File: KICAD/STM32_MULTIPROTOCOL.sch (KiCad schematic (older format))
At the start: 76 parts, among them T1 TestPoint, T10 TestPoint, T11 TestPoint, T12 TestPoint, T13 TestPoint, T14 TestPoint, T2 TestPoint, T3 TestPoint, T4 TestPoint, T5 TestPoint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

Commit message: uart,spi,iic pins init in input mode. USB enable fixed.
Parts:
- added R24: 1.5k, Resistor_SMD:R_0805_2012Metric_Pad1.15x1.40mm_HandSolder, symbol Device:R
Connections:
- net USB_DATA+: now also R24.2
- net at U2.43 (PA10): now also R24.1
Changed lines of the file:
@@
 	1    0    0    -1
 $EndComp
-Text GLabel 9200 2350 2    50   Input ~ 0
+Text GLabel 10300 2350 2    50   Input ~ 0
 USB_DATA+
-Text GLabel 9200 2250 2    50   Input ~ 0
+Text GLabel 10300 2250 2    50   Input ~ 0
 USB_DATA-
 $Comp
@@
 Connection ~ 8400 850
 Wire Wire Line
-	9200 2250 9000 2250
-Wire Wire Line
-	9000 2350 9200 2350
+	10300 2250 9000 2250
+Wire Wire Line
+	9000 2350 9950 2350
 Text GLabel 9250 1350 2    50   Input ~ 0
 UART2_TX_PA2_PIN16
@@
 	4950 7150 6850 7150
 $Comp
-L Device:R R21
-U 1 1 60ADF8C6
-P 5750 7250
-F 0 "R21" V 5750 7250 50  0000 C CNN
-F 1 "100R" V 5866 7250 50  0001 C CNN
-F 2 "Resistor_SMD:R_0805_2012Metric_Pad1.15x1.40mm_HandSolder" V 5680 7250 50  0001 C CNN
-F 3 "~" H 5750 7250 50  0001 C CNN
-	1    5750 7250
-	0    -1   -1   0
-$EndComp
-Wire Wire Line
-	5150 7250 5600 7250
-Connection ~ 5150 7250
-Wire Wire Line
-	5900 7250 6300 7250
-$Comp
 L Connector:TestPoint T13
 U 1 1 60B0CABD
@@
 P 5200 5500
 F 0 "R22" V 5200 5500 50  0000 C CNN
-F 1 "10kR" V 5316 5500 50  0001 C CNN
+F 1 "10kR" V 5316 5500 50  0000 C CNN
 F 2 "Resistor_SMD:R_0805_2012Metric_Pad1.15x1.40mm_HandSolder" V 5130 5500 50  0001 C CNN
 F 3 "~" H 5200 5500 50  0001 C CNN
@@
 P 5000 5500
 F 0 "R23" V 5000 5500 50  0000 C CNN
-F 1 "10kR" V 5116 5500 50  0001 C CNN
+F 1 "10kR" V 4900 5500 50  0000 C CNN
 F 2 "Resistor_SMD:R_0805_2012Metric_Pad1.15x1.40mm_HandSolder" V 4930 5500 50  0001 C CNN
 F 3 "~" H 5000 5500 50  0001 C CNN
@@
 U 1 1 6050A09D
 P 10250 6200
-F 0 "CF4" H 10365 6246 50  0000 L CNN
-F 1 "22pF" H 10365 6155 50  0000 L CNN
+F 0 "CF4" V 10450 6150 50  0000 L CNN
+F 1 "22pF" V 10365 6155 50  0000 L CNN
 F 2 "Resistor_SMD:R_0402_1005Metric" H 10288 6050 50  0001 C CNN
 F 3 "~" H 10250 6200 50  0001 C CNN
@@
 U 1 1 6050AC37
 P 10300 5750
-F 0 "CF3" H 10415 5796 50  0000 L CNN
-F 1 "22pF" H 10415 5705 50  0000 L CNN
+F 0 "CF3" V 10500 5700 50  0000 L CNN
+F 1 "22pF" V 10415 5705 50  0000 L CNN
 F 2 "Resistor_SMD:R_0402_1005Metric" H 10338 5600 50  0001 C CNN
 F 3 "~" H 10300 5750 50  0001 C CNN
@@
 	8600 850  8500 850
 Connection ~ 8500 850
+Connection ~ 5150 7250
+Wire Wire Line
+	5900 7250 6300 7250
+Wire Wire Line
+	5150 7250 5600 7250
+$Comp
+L Device:R R21
+U 1 1 60ADF8C6
+P 5750 7250
+F 0 "R21" V 5750 7250 50  0000 C CNN
+F 1 "100R" V 5866 7250 50  0001 C CNN
+F 2 "Resistor_SMD:R_0805_2012Metric_Pad1.15x1.40mm_HandSolder" V 5680 7250 50  0001 C CNN
+F 3 "~" H 5750 7250 50  0001 C CNN
+	1    5750 7250
+	0    -1   -1   0
+$EndComp
+Wire Wire Line
+	9550 2150 9950 2150
+$Comp
+L Device:R R24
+U 1 1 61A28BFD
+P 9400 2150
+F 0 "R24" V 9400 2150 50  0000 C CNN
+F 1 "1.5k" V 9516 2150 50  0000 C CNN
+F 2 "Resistor_SMD:R_0805_2012Metric_Pad1.15x1.40mm_HandSolder" V 9330 2150 50  0001 C CNN
+F 3 "~" H 9400 2150 50  0001 C CNN
+	1    9400 2150
+	0    -1   -1   0
+$EndComp
+Wire Wire Line
+	9000 2150 9250 2150
+Wire Wire Line
+	9950 2150 9950 2350
+Connection ~ 9950 2350
+Wire Wire Line
+	9950 2350 10300 2350
 $EndSCHEMATC

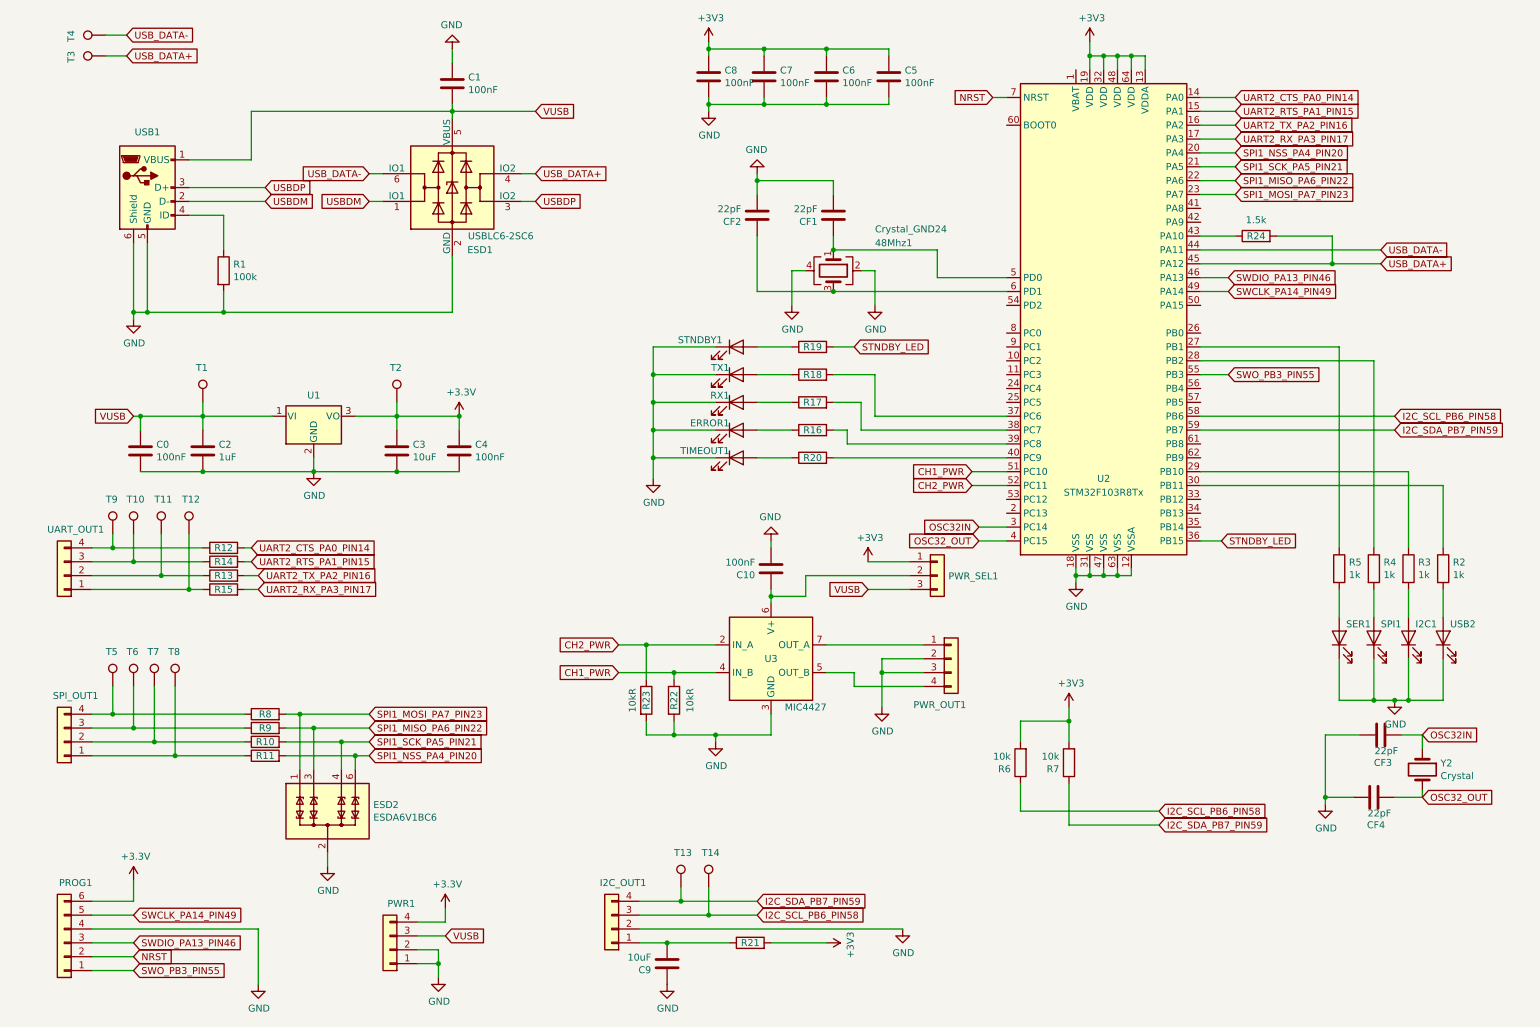
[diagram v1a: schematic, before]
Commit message: added command "stm-testled" for soldering, added schematic.pdf
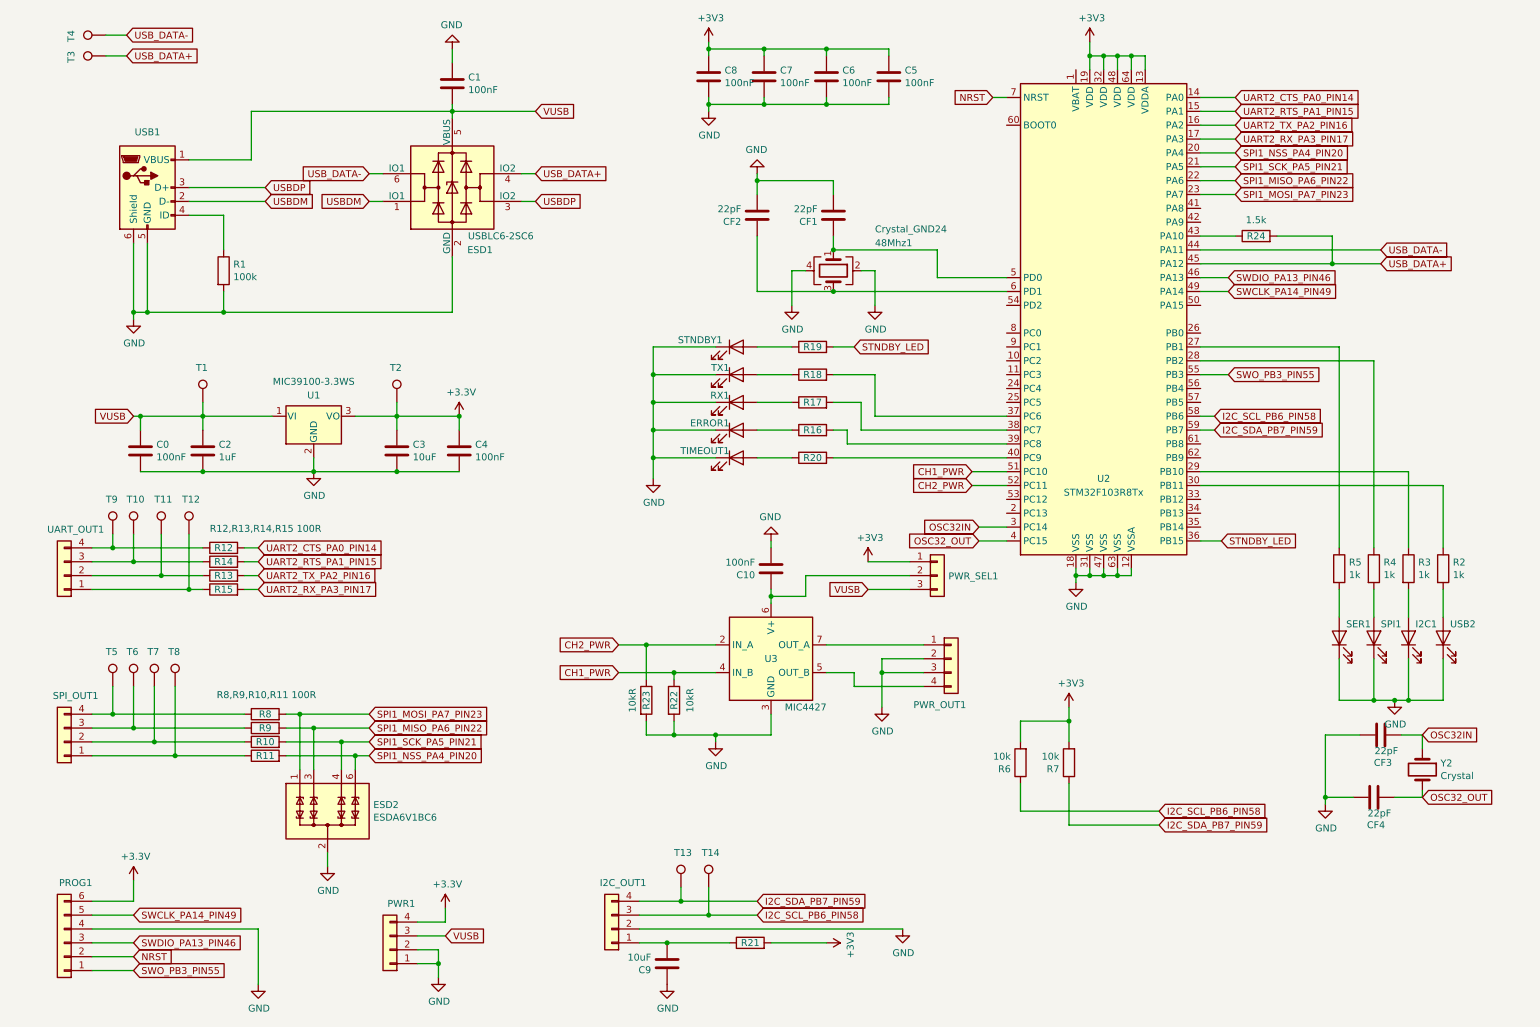
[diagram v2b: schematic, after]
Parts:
- U1: value MCP1703A-1202_SOT223 -> MIC39100-3.3WS
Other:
- note added: "R12,R13,R14,R15 100R"
- note added: "R8,R9,R10,R11 100R"
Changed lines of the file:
@@
 Wire Wire Line
 	9250 1450 9000 1450
-Text GLabel 10400 3550 2    50   Input ~ 0
+Text GLabel 9100 3550 2    50   Input ~ 0
 I2C_SDA_PB7_PIN59
-Text GLabel 10400 3450 2    50   Input ~ 0
+Text GLabel 9100 3450 2    50   Input ~ 0
 I2C_SCL_PB6_PIN58
 $Comp
@@
 P 2600 3450
 F 0 "U1" H 2600 3601 50  0000 C CNN
-F 1 "MCP1703A-1202_SOT223" H 2600 3601 50  0001 C CNN
+F 1 "MIC39100-3.3WS" H 2600 3700 50  0000 C CNN
 F 2 "Package_TO_SOT_SMD:SOT-223-3_TabPin2" H 2600 3650 50  0001 C CNN
 F 3 "http://ww1.microchip.com/downloads/en/DeviceDoc/20005122B.pdf" H 2600 3400 50  0001 C CNN
@@
 Text GLabel 2200 4700 2    50   Input ~ 0
 UART2_RX_PA3_PIN17
-Text GLabel 2150 4400 2    50   Input ~ 0
+Text GLabel 2200 4400 2    50   Input ~ 0
 UART2_CTS_PA0_PIN14
-Text GLabel 2150 4500 2    50   Input ~ 0
+Text GLabel 2200 4500 2    50   Input ~ 0
 UART2_RTS_PA1_PIN15
 Wire Wire Line
@@
 $EndComp
 Wire Wire Line
-	10400 3450 9000 3450
-Wire Wire Line
-	9000 3550 10400 3550
+	9100 3450 9000 3450
+Wire Wire Line
+	9000 3550 9100 3550
 Text GLabel 8700 6400 2    50   Input ~ 0
 I2C_SDA_PB7_PIN59
@@
 	2100 4700 2200 4700
 Wire Wire Line
-	2100 4400 2150 4400
-Wire Wire Line
-	2100 4500 2150 4500
+	2100 4400 2200 4400
+Wire Wire Line
+	2100 4500 2200 4500
 Wire Wire Line
 	3200 3350 3200 3450
@@
 Wire Wire Line
 	9950 2350 10300 2350
+Text Notes 1850 4300 0    50   ~ 0
+R12,R13,R14,R15 100R
+Text Notes 1900 5500 0    50   ~ 0
+R8,R9,R10,R11 100R
 $EndSCHEMATC

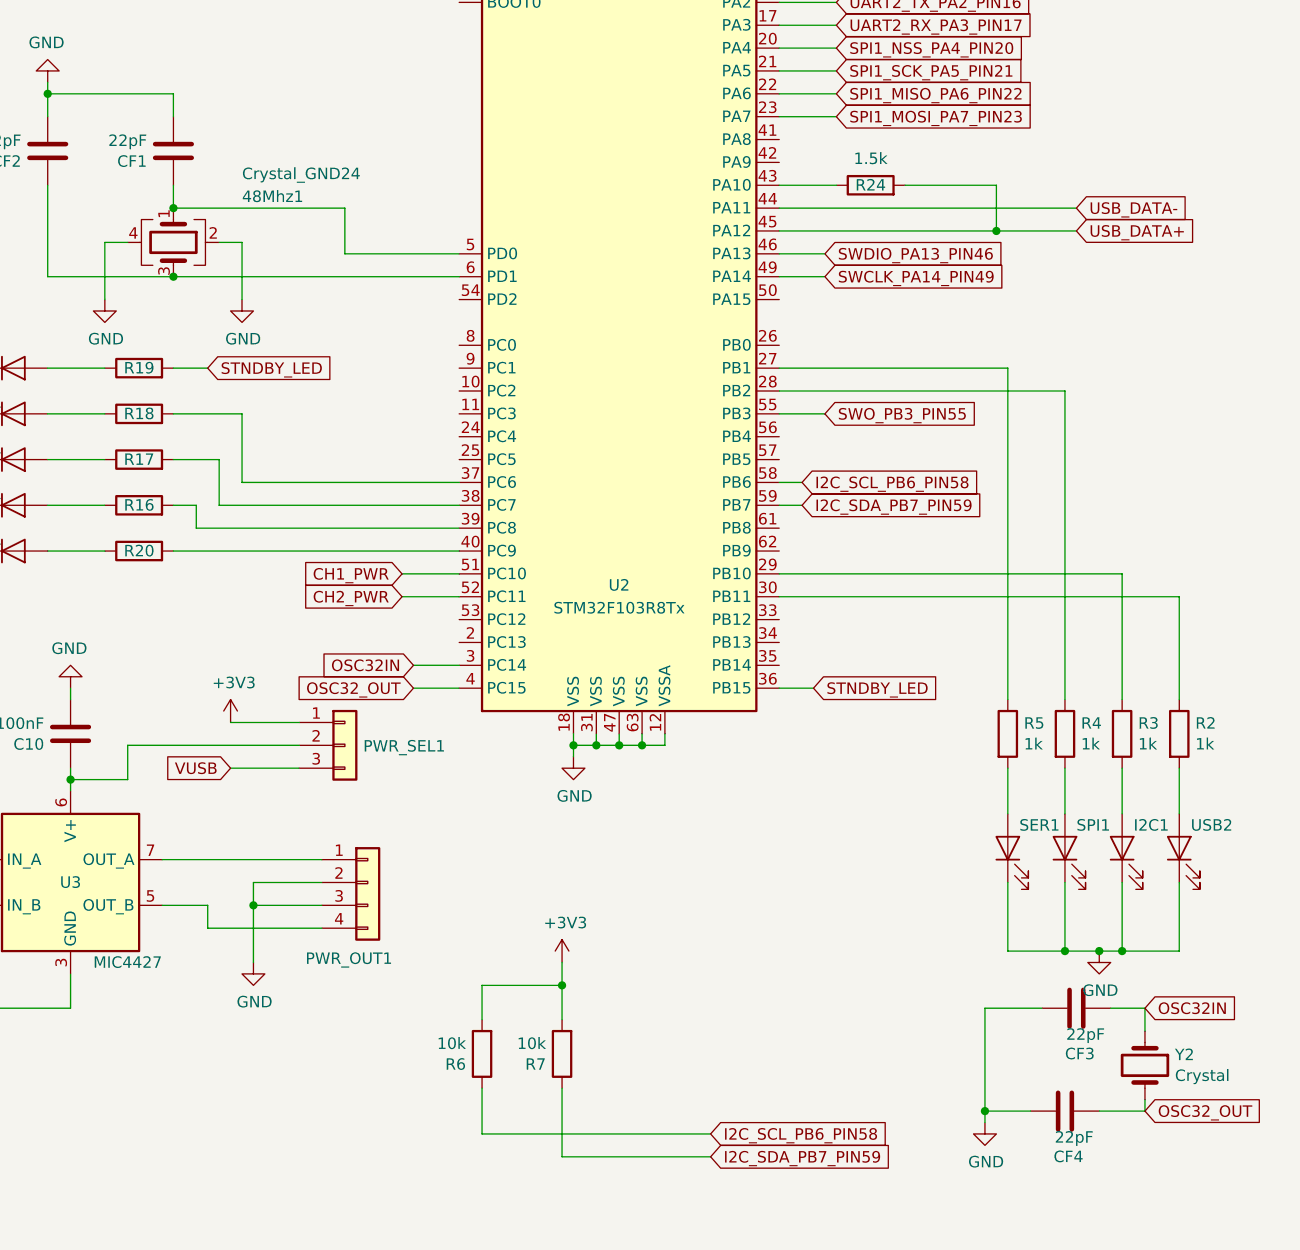
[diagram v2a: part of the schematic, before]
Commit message: added detailed BOM of the boards
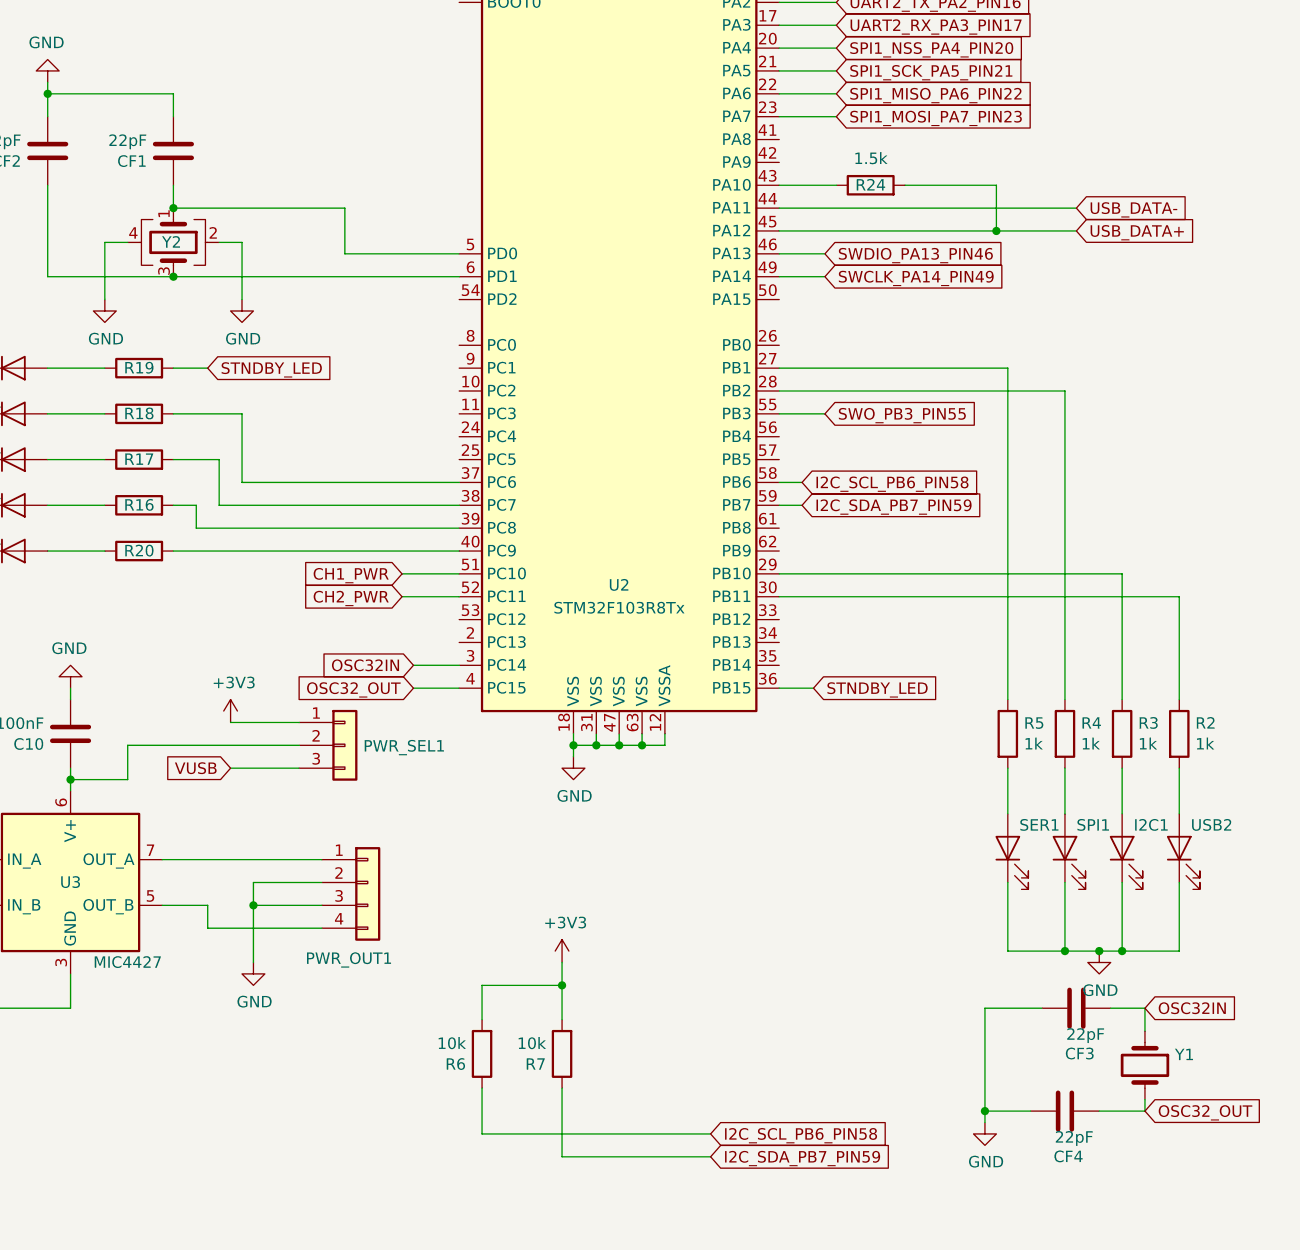
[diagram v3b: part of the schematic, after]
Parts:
- renumbered Y2 to Y1, 48Mhz1 to Y2
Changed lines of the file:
@@
 	6050 2400 6150 2400
 $Comp
-L Device:Crystal_GND24 48Mhz1
+L Device:Crystal_GND24 Y2
 U 1 1 604D9F9D
 P 6350 2400
-F 0 "48Mhz1" V 6150 2700 50  0000 L CNN
-F 1 "Crystal_GND24" V 6050 2700 50  0000 L CNN
+F 0 "Y2" V 6350 2350 50  0000 L CNN
+F 1 "Crystal_GND24" V 6050 2700 50  0001 L CNN
 F 2 "Crystal:Crystal_SMD_3225-4Pin_3.2x2.5mm" H 6350 2400 50  0001 C CNN
 F 3 "~" H 6350 2400 50  0001 C CNN
@@
 Connection ~ 6350 2250
 $Comp
-L Device:Crystal Y2
+L Device:Crystal Y1
 U 1 1 60507E51
 P 10600 6000
-F 0 "Y2" V 10554 6131 50  0000 L CNN
-F 1 "Crystal" V 10645 6131 50  0000 L CNN
+F 0 "Y1" V 10554 6131 50  0000 L CNN
+F 1 "Crystal" V 10645 6131 50  0001 L CNN
 F 2 "Crystal:Crystal_SMD_TXC_9HT11-2Pin_2.0x1.2mm_HandSoldering" H 10600 6000 50  0001 C CNN
 F 3 "~" H 10600 6000 50  0001 C CNN
